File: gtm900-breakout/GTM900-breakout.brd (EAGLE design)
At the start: 70 x 70 mm, 96 parts, among them J1 AUDIO-JACK3, K1 694108106102, T1 BC847, T2 BC847, T3 BC847, T4 BC847, U1 FH12A-40S-0.5SH(55), U3 MCP1827T-ADJE/ET, U4 MIC5366, U5 CP2105-GM, U6 IP4234CZ6, X4 MINI-USB-SHIELD-UX60-MB-5ST

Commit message: gtm900-bo: ERC + DRC done + corrections
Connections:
- removed net N$15: R4.2
- net VIO_2V8: now also R4.2
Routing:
- net VIO_2V8: track 83.5 -> 137.4 mm
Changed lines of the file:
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@@
 <layer number="19" name="Unrouted" color="6" fill="1" visible="yes" active="yes"/>
 <layer number="20" name="Dimension" color="15" fill="1" visible="yes" active="yes"/>
-<layer number="21" name="tPlace" color="7" fill="1" visible="yes" active="yes"/>
-<layer number="22" name="bPlace" color="7" fill="1" visible="yes" active="yes"/>
-<layer number="23" name="tOrigins" color="15" fill="1" visible="yes" active="yes"/>
-<layer number="24" name="bOrigins" color="15" fill="1" visible="yes" active="yes"/>
+<layer number="21" name="tPlace" color="7" fill="1" visible="no" active="yes"/>
+<layer number="22" name="bPlace" color="7" fill="1" visible="no" active="yes"/>
+<layer number="23" name="tOrigins" color="15" fill="1" visible="no" active="yes"/>
+<layer number="24" name="bOrigins" color="15" fill="1" visible="no" active="yes"/>
 <layer number="25" name="tNames" color="7" fill="1" visible="yes" active="yes"/>
 <layer number="26" name="bNames" color="7" fill="1" visible="yes" active="yes"/>
 <layer number="27" name="tValues" color="7" fill="1" visible="no" active="yes"/>
 <layer number="28" name="bValues" color="7" fill="1" visible="no" active="yes"/>
-<layer number="29" name="tStop" color="7" fill="3" visible="yes" active="yes"/>
+<layer number="29" name="tStop" color="7" fill="3" visible="no" active="yes"/>
 <layer number="30" name="bStop" color="7" fill="6" visible="no" active="yes"/>
 <layer number="31" name="tCream" color="7" fill="4" visible="no" active="yes"/>
@@
 <layer number="37" name="tTest" color="7" fill="1" visible="yes" active="yes"/>
 <layer number="38" name="bTest" color="7" fill="1" visible="no" active="yes"/>
-<layer number="39" name="tKeepout" color="4" fill="11" visible="yes" active="yes"/>
+<layer number="39" name="tKeepout" color="4" fill="11" visible="no" active="yes"/>
 <layer number="40" name="bKeepout" color="1" fill="11" visible="no" active="yes"/>
-<layer number="41" name="tRestrict" color="4" fill="10" visible="yes" active="yes"/>
+<layer number="41" name="tRestrict" color="4" fill="10" visible="no" active="yes"/>
 <layer number="42" name="bRestrict" color="1" fill="10" visible="no" active="yes"/>
-<layer number="43" name="vRestrict" color="2" fill="10" visible="yes" active="yes"/>
+<layer number="43" name="vRestrict" color="2" fill="10" visible="no" active="yes"/>
 <layer number="44" name="Drills" color="7" fill="1" visible="no" active="yes"/>
-<layer number="45" name="Holes" color="7" fill="1" visible="yes" active="yes"/>
+<layer number="45" name="Holes" color="7" fill="1" visible="no" active="yes"/>
 <layer number="46" name="Milling" color="3" fill="1" visible="no" active="yes"/>
 <layer number="47" name="Measures" color="7" fill="1" visible="yes" active="yes"/>
@@
 <via x="4.699" y="43.18" extent="1-16" drill="0.3"/>
 <via x="33.5915" y="13.3985" extent="1-16" drill="0.3"/>
-<via x="33.274" y="24.8285" extent="1-16" drill="0.3"/>
+<via x="36.449" y="24.8285" extent="1-16" drill="0.3"/>
 <via x="26.289" y="21.0185" extent="1-16" drill="0.3"/>
 <via x="18.669" y="21.0185" extent="1-16" drill="0.3"/>
@@
 <wire x1="17.145" y1="24.638" x2="17.145" y2="25.908" width="0.3048" layer="1"/>
 <wire x1="1.2" y1="23.368" x2="0.508" y2="23.368" width="0.254" layer="1"/>
+<contactref element="R4" pad="2"/>
+<wire x1="31.877" y1="59.055" x2="31.877" y2="59.182" width="0.3048" layer="1"/>
+<wire x1="31.877" y1="59.182" x2="33.02" y2="60.325" width="0.3048" layer="1"/>
+<wire x1="33.02" y1="60.325" x2="37.465" y2="60.325" width="0.3048" layer="1"/>
+<wire x1="37.465" y1="60.325" x2="41.275" y2="56.515" width="0.3048" layer="1"/>
+<wire x1="41.275" y1="56.515" x2="41.275" y2="26.67" width="0.3048" layer="1"/>
+<wire x1="41.275" y1="26.67" x2="40.64" y2="26.035" width="0.3048" layer="1"/>
+<wire x1="40.64" y1="26.035" x2="36.195" y2="26.035" width="0.3048" layer="1"/>
+<wire x1="36.195" y1="26.035" x2="35.56" y2="25.4" width="0.3048" layer="1"/>
+<wire x1="35.56" y1="25.4" x2="31.115" y2="25.4" width="0.3048" layer="1"/>
+<wire x1="31.115" y1="25.4" x2="29.845" y2="24.13" width="0.3048" layer="1"/>
 </signal>
 <signal name="N$10">
@@
 <wire x1="30.282" y1="58.984" x2="30.353" y2="59.055" width="0.3048" layer="1"/>
 </signal>
-<signal name="N$15">
-<contactref element="R4" pad="2"/>
-</signal>
 <signal name="GPIO.1_ECI/DSR_ECI">

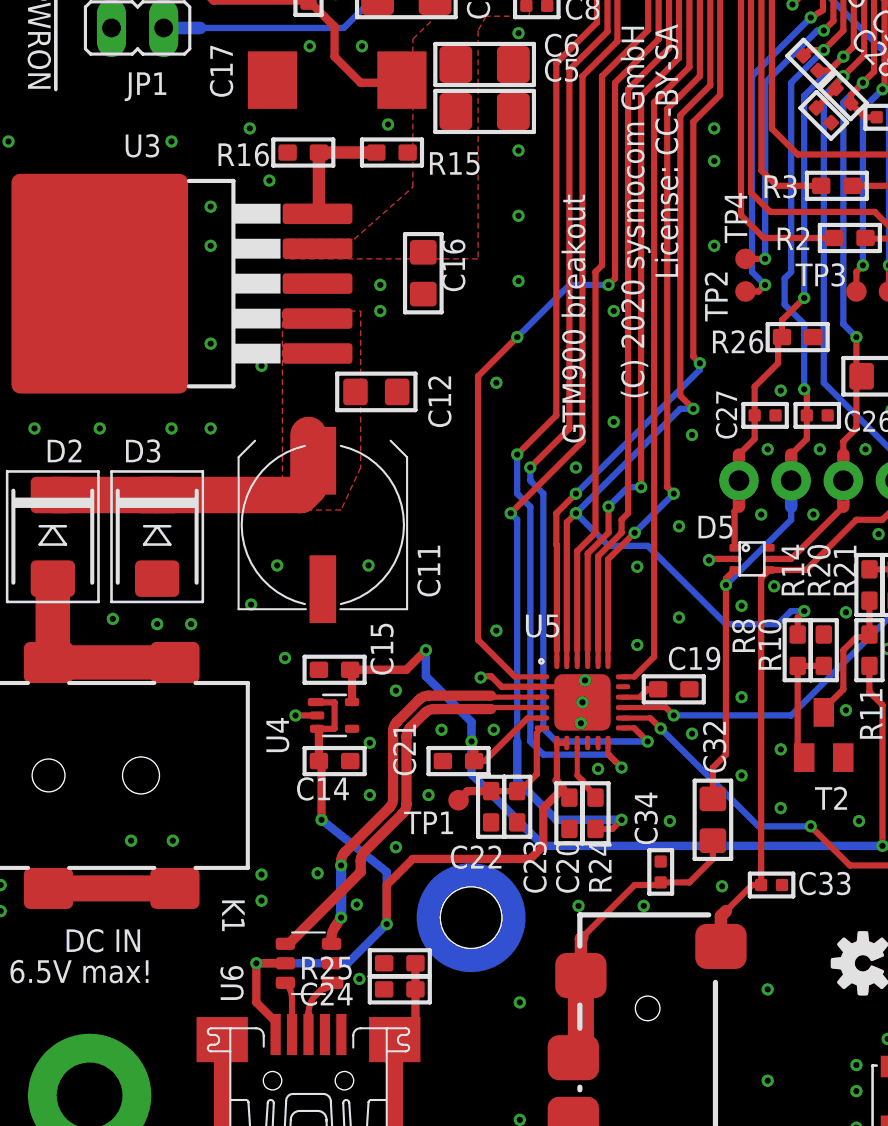
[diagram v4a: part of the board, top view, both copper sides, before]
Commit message: gtm900-bo: re-introduce serial 0R on UART_RI
...not, that it was needed, but just in case...
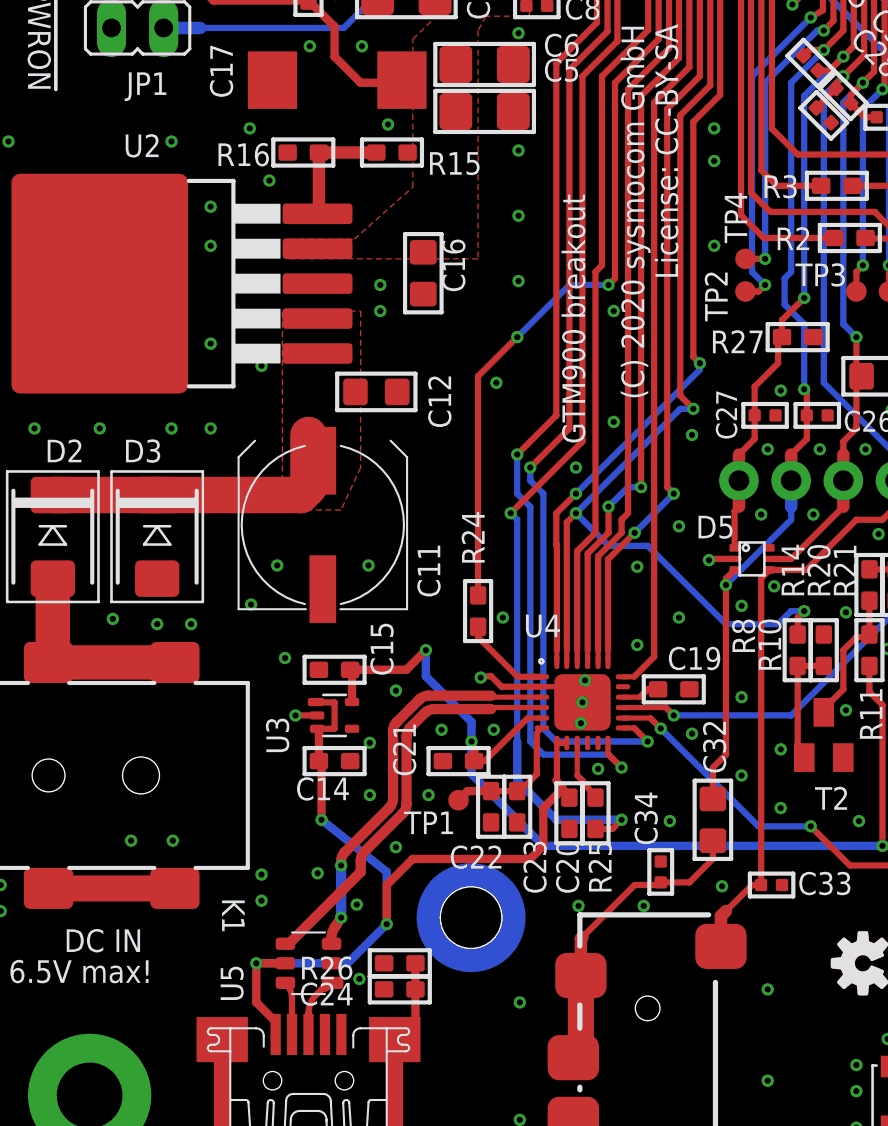
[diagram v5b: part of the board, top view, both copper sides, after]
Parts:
- removed U6: IP4234CZ6, laforge:TSOP-6
- added R27: 0, rc-sysmocom:_0603@1
- added U2: MCP1827T-ADJE/ET, ldo:TI_KTT_DPAK2
- R24: value 4.7k -> 0
- R25: value 1M -> 4.7k
- R26: value 0 -> 1M
- U3: value MCP1827T-ADJE/ET -> MIC5366; device ldo:TI_KTT_DPAK2 -> ldo:SC70-5
- U4: value MIC5366 -> CP2105-GM; device ldo:SC70-5 -> usb-uart:QFN24_4X4
- U5: value CP2105-GM -> IP4234CZ6; device usb-uart:QFN24_4X4 -> laforge:TSOP-6
- moved R26 36.1 mm to (-5.71, 11.4), turned to 0 degrees
- moved U3 23.9 mm to (-8.89, 23.5), turned to 270 degrees
- moved U5 18.4 mm to (-10.2, 11.4), turned to 90 degrees
- moved U4 12.1 mm to (3.17, 24.1), turned to 0 degrees
- moved R25 12.0 mm to (3.81, 18.7), turned to 270 degrees
- moved R24 11.4 mm to (-1.91, 28.6)
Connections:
- new net N$15: R24.2, U4.1
- net EAR-: now also R27.2; no longer R26.2
- net GND: now also R27.1, U2.3, U2.PAD, U3.2, U4.25; no longer R25.1, U3.3, U3.PAD, U5.25, U6.2
- net GPIO.0_ECI/DTR_ECI: now also U4.15; no longer U5.15
- net GPIO.1_ECI/DSR_ECI: now also U4.14; no longer U5.14
- net LDO_IN: now also U2.1, U2.2; no longer U3.1, U3.2
- net N$11: now also R26.2; no longer R25.2
- net N$12: now also R25.1, U4.9; no longer R24.1, U5.9
- net N$14: now also U4.16; no longer U5.16
- net N$6: now also U2.5; no longer U3.5
- net RXD2: now also U4.12; no longer U5.12
- net TXD2: now also U4.13; no longer U5.13
- net UART_CTS: now also U4.18; no longer U5.18
- net UART_DCD: now also U4.24; no longer U5.24
- net UART_DSR: now also U4.22; no longer U5.22
- net UART_DTR: now also U4.23; no longer U5.23
- net UART_RI: now also R24.1; no longer U5.1
- net UART_RTS: now also U4.19; no longer U5.19
- net UART_RXD: now also U4.20; no longer U5.20
- net UART_TXD: now also U4.21; no longer U5.21
- net USB_D_N: now also U4.4; no longer U6.4
- net USB_D_P: now also U4.3; no longer U6.3
- net USB_VBUS: now also U3.1, U3.3, U4.7, U4.8, U5.5; no longer U4.1, U4.3, U5.7, U5.8, U6.5
- net VCC: now also U2.4; no longer U3.4
- net VDD: now also R25.2; no longer R24.2
- net VDD_3V45: now also U4.6; no longer U5.6
- net VIO_2V8: now also U3.5; no longer U5.5
- net _USB_DN: now also U5.6; no longer U6.6
- net _USB_DP: now also U5.1; no longer U6.1
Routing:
- net UART_RI: track 43.0 -> 37.0 mm
- net N$15: track 0.00 -> 4.41 mm

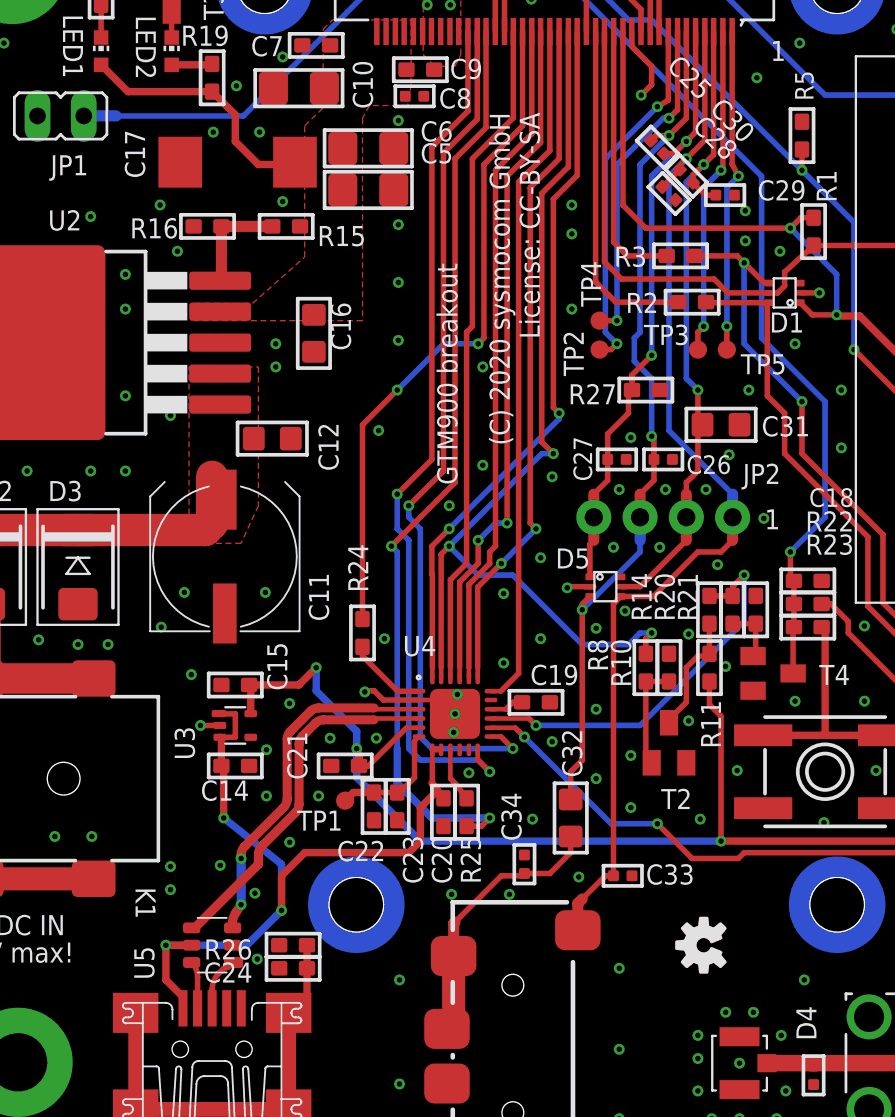
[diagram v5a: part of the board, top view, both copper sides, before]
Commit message: gtm900-bo: ease some part's distances, increase OSHW logo
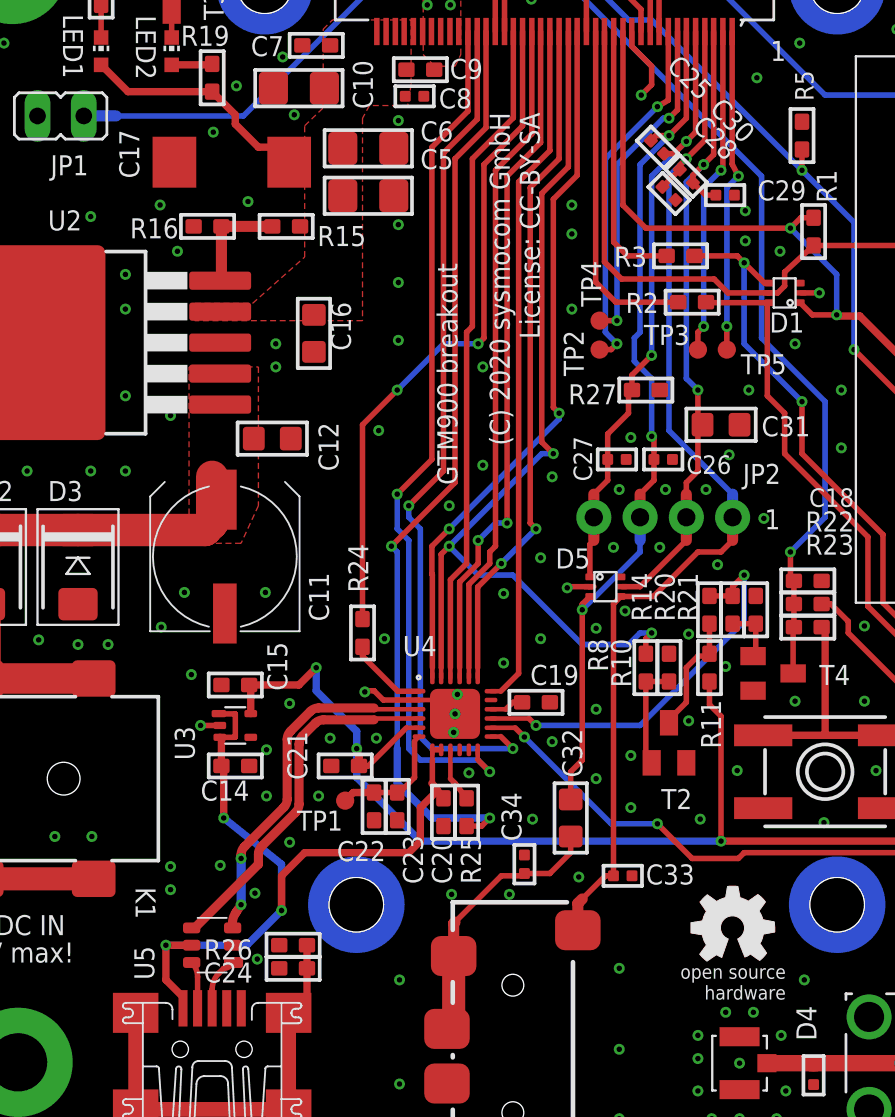
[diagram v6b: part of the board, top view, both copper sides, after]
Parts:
- removed LOGO3: OSHW-LOGOS-COPPER, SparkFun-Aesthetics:OSHW-LOGO-S_COPPER
- U$3: device SparkFun-Aesthetics:OSHW-LOGO-S -> oshw:OSHW_5MM_COPPER
- moved U$3 1.85 mm to (18.4, 12.4), turned to 0 degrees
- moved C17 0.32 mm to (-9.08, 54.4)
- moved C5 0.32 mm to (-1.59, 52.6)
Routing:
- net VCC: track 13.8 -> 13.3 mm

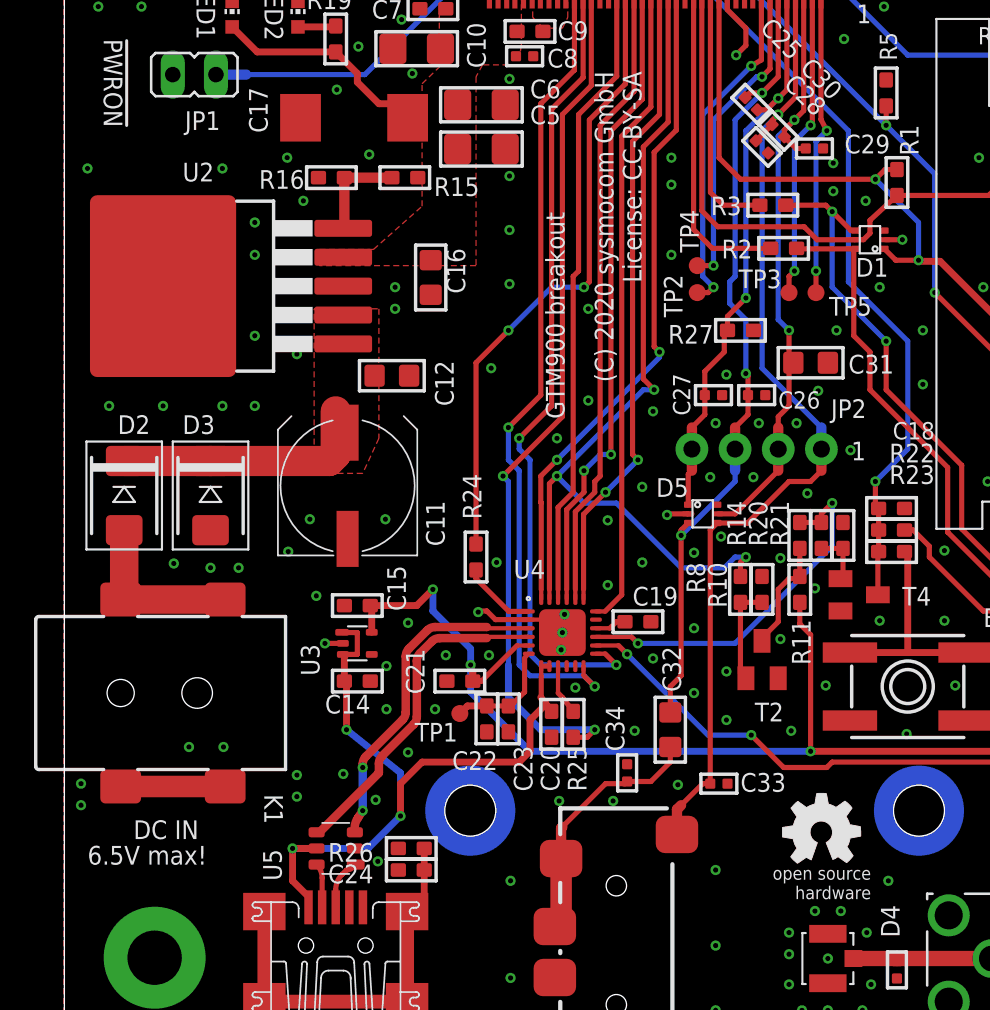
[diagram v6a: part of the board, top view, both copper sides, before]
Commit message: gtm900-bo: add header for power source selection (DC in / USB)
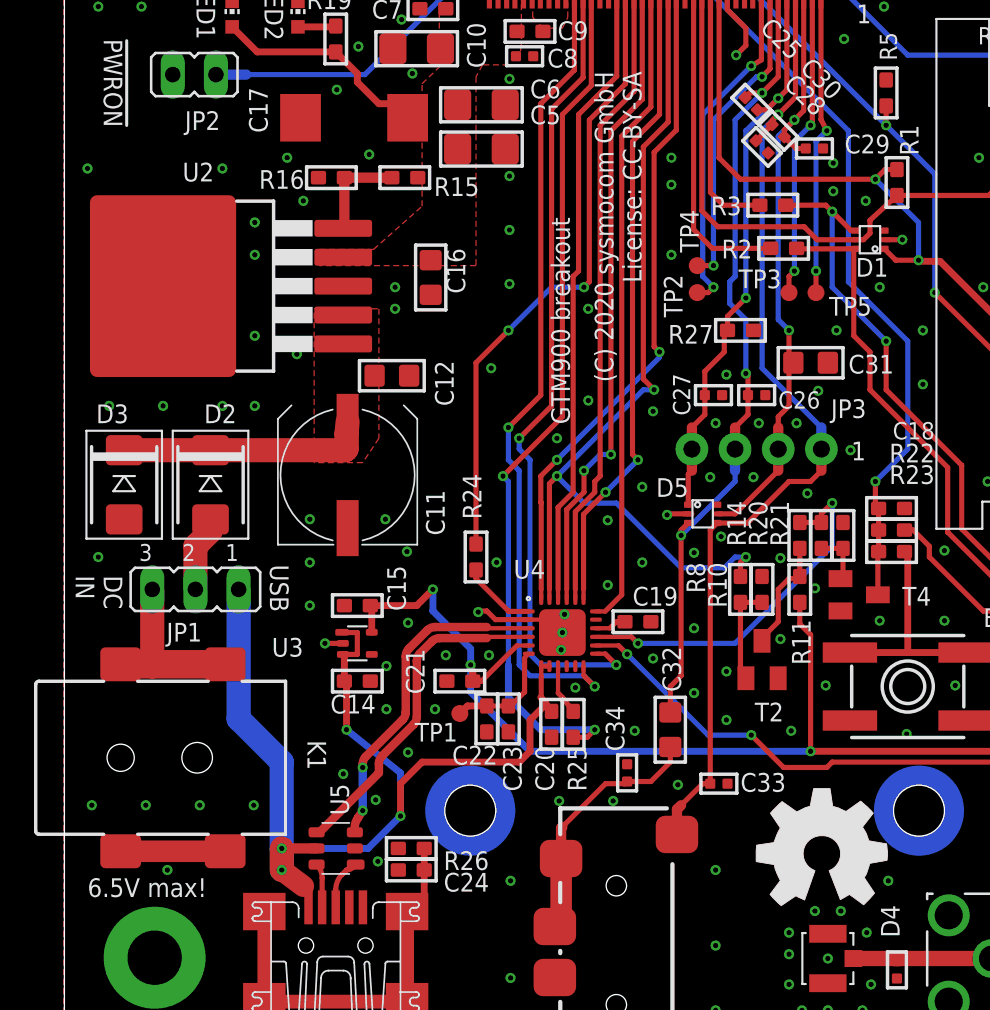
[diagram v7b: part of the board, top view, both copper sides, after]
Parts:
- added JP3: (no value), microbuilder:1X04_ROUND_76
- JP1: device jumper:JP1 -> jumper:JP2
- JP2: device microbuilder:1X04_ROUND_76 -> jumper:JP1
- U$3: device oshw:OSHW_5MM_COPPER -> oshw:OSHW_8MM_COPPER
- moved JP2 39.7 mm to (-18.5, 57.0), turned to 90 degrees
- moved JP1 30.3 mm to (-18.4, 26.7), turned to 180 degrees
- moved D2 5.12 mm to (-17.5, 32.8)
- moved D3 5.12 mm to (-22.6, 32.8)
- moved K1 3.81 mm to (-27.8, 16.8)
- moved U$3 1.27 mm to (18.4, 11.1)
- moved C11 0.64 mm to (-9.46, 33.4)
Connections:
- new net N$19: D2.A, JP1.2
- net !PWON: now also JP2.1; no longer JP1.1
- net EAR+: now also JP3.3; no longer JP2.3
- net EAR-: now also JP3.4; no longer JP2.4
- net GND: now also JP2.2; no longer JP1.2
- net MIC+: now also JP3.1; no longer JP2.1
- net MIC-: now also JP3.2; no longer JP2.2
- net N$4: now also JP1.3; no longer D2.A
- net USB_VBUS: now also JP1.1
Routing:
- net USB_VBUS: track 43.4 -> 62.6 mm, vias 3 -> 4
- net N$19: track 0.00 -> 4.49 mm
- net GND: vias 167 -> 165
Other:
- board text added: "USB"

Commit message: gtm900-bo: update parts to avail @Digikey, upd all ext'd attribs
... in sch and brd too
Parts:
- D2: value SD2114S040S5R0 -> ACDBB540-HF
- K1: value 694108106102 -> PJ-002BH-SMT-TR
- R1, R10, R11, R12, R13, R14, R15, R16, R17, R18, R19, R2, R20, R21, R22, R23, R24, R25, R26, R27, R3, R4, R5, R6, R7, R8, R9: device rc-sysmocom:_0603@1 -> rc-sysmocom:_0603
